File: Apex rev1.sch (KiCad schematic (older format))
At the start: 10 parts

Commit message: Update matrix and MCU
Updated matrix. Added decoupling capacitors. Added Encoder.
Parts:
- added C?: 1uF, symbol Device:C
- added C?: 4.7u, symbol Device:C_Small
- added C? (x4): .1u, symbol Device:C_Small
- added SW?: Rotary_Encoder, symbol Device:Rotary_Encoder
- R?: symbol keyboard_parts:R -> Apex-rev1-rescue:R-keyboard_parts
- SW?: symbol keyboard_parts:SW_PUSH -> Apex-rev1-rescue:SW_PUSH-keyboard_parts
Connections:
- net labels added: ENC1, ENC2
- wire segments 33 -> 49
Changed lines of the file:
@@
 	8400 1750 8250 1750
 $Comp
-L keyboard_parts:R R?
+L Apex-rev1-rescue:R-keyboard_parts R?
 U 1 1 5EFE3710
 P 8250 1500
@@
 Connection ~ 8250 1750
 $Comp
-L keyboard_parts:SW_PUSH SW?
+L Apex-rev1-rescue:SW_PUSH-keyboard_parts SW?
 U 1 1 5EFE4C93
 P 7800 1750
@@
 	8900 5450 8950 5450
 Wire Wire Line
-	8950 5450 8950 5500
+	8950 5450 8950 5800
 Connection ~ 8950 5450
 Wire Wire Line
@@
 L power:GND #PWR?
 U 1 1 5F0428AB
-P 8950 5500
-F 0 "#PWR?" H 8950 5250 50  0001 C CNN
-F 1 "GND" H 8955 5327 50  0000 C CNN
-F 2 "" H 8950 5500 50  0001 C CNN
-F 3 "" H 8950 5500 50  0001 C CNN
-	1    8950 5500
+P 8950 5800
+F 0 "#PWR?" H 8950 5550 50  0001 C CNN
+F 1 "GND" H 8955 5627 50  0000 C CNN
+F 2 "" H 8950 5800 50  0001 C CNN
+F 3 "" H 8950 5800 50  0001 C CNN
+	1    8950 5800
 	1    0    0    -1
 $EndComp
@@
 F1 "Key Matrix.sch" 50
 $EndSheet
+Wire Wire Line
+	8400 3050 7650 3050
+$Comp
+L Device:C C?
+U 1 1 5F07097E
+P 7650 3200
+F 0 "C?" H 7765 3246 50  0000 L CNN
+F 1 "1uF" H 7765 3155 50  0000 L CNN
+F 2 "" H 7688 3050 50  0001 C CNN
+F 3 "~" H 7650 3200 50  0001 C CNN
+	1    7650 3200
+	1    0    0    -1
+$EndComp
+Wire Wire Line
+	7650 3350 7650 3450
+$Comp
+L power:GND #PWR?
+U 1 1 5F071BD0
+P 7650 3450
+F 0 "#PWR?" H 7650 3200 50  0001 C CNN
+F 1 "GND" H 7655 3277 50  0000 C CNN
+F 2 "" H 7650 3450 50  0001 C CNN
+F 3 "" H 7650 3450 50  0001 C CNN
+	1    7650 3450
+	1    0    0    -1
+$EndComp
+Wire Wire Line
+	8400 2550 7950 2550
+Connection ~ 7950 2550
+Wire Wire Line
+	7950 2550 7150 2550
+$Comp
+L power:VCC #PWR?
+U 1 1 5F073B72
+P 7150 2550
+F 0 "#PWR?" H 7150 2400 50  0001 C CNN
+F 1 "VCC" H 7165 2723 50  0000 C CNN
+F 2 "" H 7150 2550 50  0001 C CNN
+F 3 "" H 7150 2550 50  0001 C CNN
+	1    7150 2550
+	1    0    0    -1
+$EndComp
+$Comp
+L Device:Rotary_Encoder SW?
+U 1 1 5F0786F9
+P 11700 2950
+F 0 "SW?" H 11930 2996 50  0000 L CNN
+F 1 "Rotary_Encoder" H 11930 2905 50  0000 L CNN
+F 2 "" H 11550 3110 50  0001 C CNN
+F 3 "~" H 11700 3210 50  0001 C CNN
+	1    11700 2950
+	1    0    0    -1
+$EndComp
+Text GLabel 11400 2850 0    50   Input ~ 0
+ENC1
+Text GLabel 11400 3050 0    50   Input ~ 0
+ENC2
+Wire Wire Line
+	11400 2950 11000 2950
+Wire Wire Line
+	11000 2950 11000 3100
+$Comp
+L power:GND #PWR?
+U 1 1 5F095086
+P 11000 3100
+F 0 "#PWR?" H 11000 2850 50  0001 C CNN
+F 1 "GND" H 11005 2927 50  0000 C CNN
+F 2 "" H 11000 3100 50  0001 C CNN
+F 3 "" H 11000 3100 50  0001 C CNN
+	1    11000 3100
+	1    0    0    -1
+$EndComp
+$Comp
+L Device:C_Small C?
+U 1 1 5F0A1E50
+P 5900 3250
+F 0 "C?" H 5992 3296 50  0000 L CNN
+F 1 "4.7u" H 5992 3205 50  0000 L CNN
+F 2 "" H 5900 3250 50  0001 C CNN
+F 3 "~" H 5900 3250 50  0001 C CNN
+	1    5900 3250
+	1    0    0    -1
+$EndComp
+$Comp
+L Device:C_Small C?
+U 1 1 5F0A2EEA
+P 5450 3250
+F 0 "C?" H 5542 3296 50  0000 L CNN
+F 1 ".1u" H 5542 3205 50  0000 L CNN
+F 2 "" H 5450 3250 50  0001 C CNN
+F 3 "~" H 5450 3250 50  0001 C CNN
+	1    5450 3250
+	1    0    0    -1
+$EndComp
+$Comp
+L Device:C_Small C?
+U 1 1 5F0A3767
+P 5000 3250
+F 0 "C?" H 5092 3296 50  0000 L CNN
+F 1 ".1u" H 5092 3205 50  0000 L CNN
+F 2 "" H 5000 3250 50  0001 C CNN
+F 3 "~" H 5000 3250 50  0001 C CNN
+	1    5000 3250
+	1    0    0    -1
+$EndComp
+$Comp
+L Device:C_Small C?
+U 1 1 5F0A3AEE
+P 4550 3250
+F 0 "C?" H 4642 3296 50  0000 L CNN
+F 1 ".1u" H 4642 3205 50  0000 L CNN
+F 2 "" H 4550 3250 50  0001 C CNN
+F 3 "~" H 4550 3250 50  0001 C CNN
+	1    4550 3250
+	1    0    0    -1
+$EndComp
+$Comp
+L Device:C_Small C?
+U 1 1 5F0A4338
+P 4200 3250
+F 0 "C?" H 4292 3296 50  0000 L CNN
+F 1 ".1u" H 4292 3205 50  0000 L CNN
+F 2 "" H 4200 3250 50  0001 C CNN
+F 3 "~" H 4200 3250 50  0001 C CNN
+	1    4200 3250
+	1    0    0    -1
+$EndComp
+Wire Wire Line
+	4200 3150 4550 3150
+Connection ~ 4550 3150
+Wire Wire Line
+	4550 3150 5000 3150
+Connection ~ 5000 3150
+Wire Wire Line
+	5000 3150 5450 3150
+Connection ~ 5450 3150
+Wire Wire Line
+	5450 3150 5900 3150
+Wire Wire Line
+	5900 3350 5450 3350
+Connection ~ 4550 3350
+Wire Wire Line
+	4550 3350 4200 3350
+Connection ~ 5000 3350
+Wire Wire Line
+	5000 3350 4550 3350
+Connection ~ 5450 3350
+Wire Wire Line
+	5450 3350 5000 3350
+Wire Wire Line
+	4200 3350 4200 3450
+Connection ~ 4200 3350
+Wire Wire Line
+	4200 3150 4200 3000
+Connection ~ 4200 3150
+$Comp
+L power:GND #PWR?
+U 1 1 5F0A7BB5
+P 4200 3450
+F 0 "#PWR?" H 4200 3200 50  0001 C CNN
+F 1 "GND" H 4205 3277 50  0000 C CNN
+F 2 "" H 4200 3450 50  0001 C CNN
+F 3 "" H 4200 3450 50  0001 C CNN
+	1    4200 3450
+	1    0    0    -1
+$EndComp
+$Comp
+L power:VCC #PWR?
+U 1 1 5F0A8382
+P 4200 3000
+F 0 "#PWR?" H 4200 2850 50  0001 C CNN
+F 1 "VCC" H 4215 3173 50  0000 C CNN
+F 2 "" H 4200 3000 50  0001 C CNN
+F 3 "" H 4200 3000 50  0001 C CNN
+	1    4200 3000
+	1    0    0    -1
+$EndComp
 $EndSCHEMATC

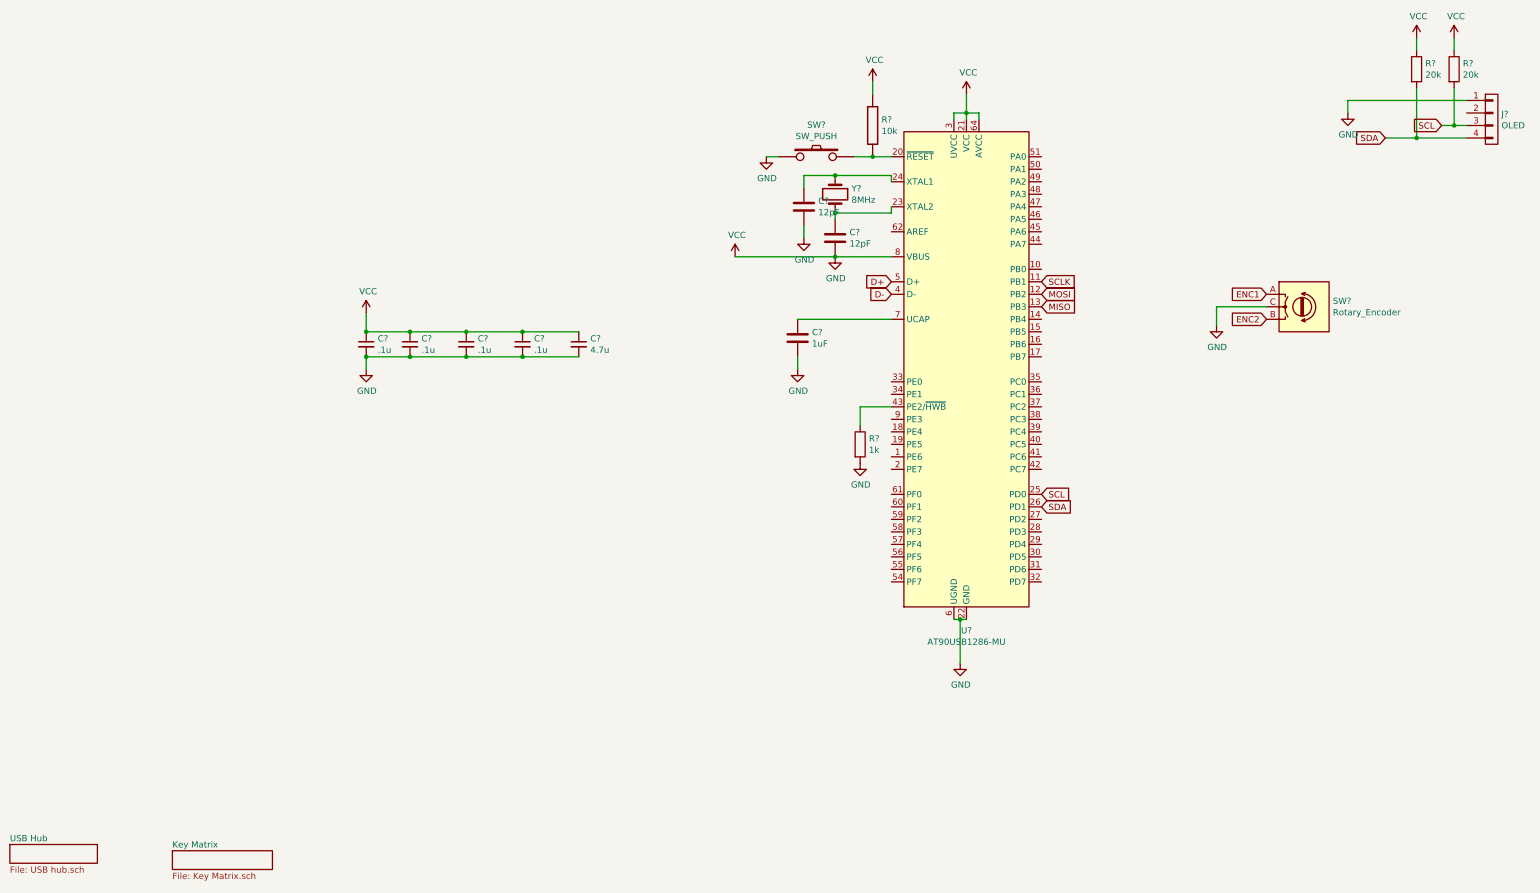
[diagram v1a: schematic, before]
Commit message: Begin annotation
Annotated schematic and began associating symbols with footprints.
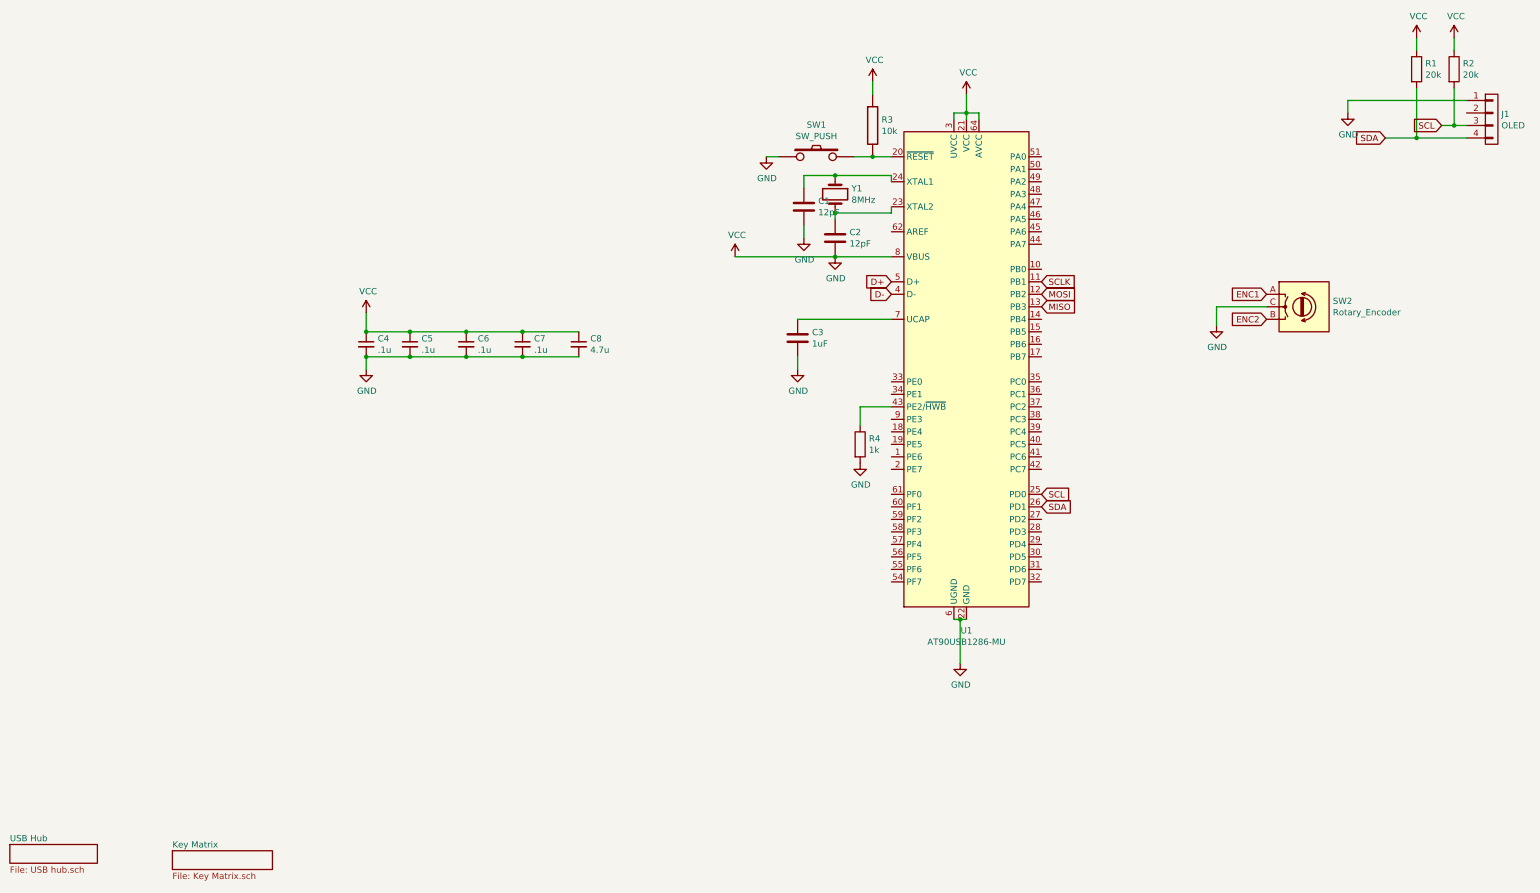
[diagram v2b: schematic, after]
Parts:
- C1, C2, C3, C4, C5, C6, C7, C8: renamed from C?; footprint (none) -> Capacitor_SMD:C_0805_2012Metric
- gave numbers to parts that had none: 9
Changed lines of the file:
@@
 $EndDescr
 $Comp
-L MCU_Microchip_AVR:AT90USB1286-MU U?
+L MCU_Microchip_AVR:AT90USB1286-MU U1
 U 1 1 5F010370
 P 9000 3450
-F 0 "U?" H 9000 1361 50  0000 C CNN
+F 0 "U1" H 9000 1361 50  0000 C CNN
 F 1 "AT90USB1286-MU" H 9000 1270 50  0000 C CNN
 F 2 "Package_DFN_QFN:QFN-64-1EP_9x9mm_P0.5mm_EP7.5x7.5mm" H 9000 3450 50  0001 C CIN
@@
 $EndComp
 $Comp
-L power:VCC #PWR?
+L power:VCC #PWR0101
 U 1 1 5F016D8A
 P 9000 1250
-F 0 "#PWR?" H 9000 1100 50  0001 C CNN
+F 0 "#PWR0101" H 9000 1100 50  0001 C CNN
 F 1 "VCC" H 9015 1423 50  0000 C CNN
 F 2 "" H 9000 1250 50  0001 C CNN
@@
 	8400 1750 8250 1750
 $Comp
-L Apex-rev1-rescue:R-keyboard_parts R?
+L Apex-rev1-rescue:R-keyboard_parts R3
 U 1 1 5EFE3710
 P 8250 1500
-F 0 "R?" H 8321 1546 50  0000 L CNN
+F 0 "R3" H 8321 1546 50  0000 L CNN
 F 1 "10k" H 8321 1455 50  0000 L CNN
-F 2 "" H 8250 1500 60  0000 C CNN
+F 2 "" H 8250 1500 60  0001 C CNN
 F 3 "" H 8250 1500 60  0000 C CNN
 	1    8250 1500
@@
 Connection ~ 8250 1750
 $Comp
-L Apex-rev1-rescue:SW_PUSH-keyboard_parts SW?
+L Apex-rev1-rescue:SW_PUSH-keyboard_parts SW1
 U 1 1 5EFE4C93
 P 7800 1750
-F 0 "SW?" H 7800 2005 50  0000 C CNN
+F 0 "SW1" H 7800 2005 50  0000 C CNN
 F 1 "SW_PUSH" H 7800 1914 50  0000 C CNN
-F 2 "" H 7800 1750 60  0000 C CNN
+F 2 "" H 7800 1750 60  0001 C CNN
 F 3 "" H 7800 1750 60  0000 C CNN
 	1    7800 1750
@@
 $EndComp
 $Comp
-L power:GND #PWR?
+L power:GND #PWR0102
 U 1 1 5EFE56D1
 P 7400 1750
-F 0 "#PWR?" H 7400 1500 50  0001 C CNN
+F 0 "#PWR0102" H 7400 1500 50  0001 C CNN
 F 1 "GND" H 7405 1577 50  0000 C CNN
 F 2 "" H 7400 1750 50  0001 C CNN
@@
 	8250 1250 8250 1150
 $Comp
-L power:VCC #PWR?
+L power:VCC #PWR0103
 U 1 1 5EFE6069
 P 8250 1150
-F 0 "#PWR?" H 8250 1000 50  0001 C CNN
+F 0 "#PWR0103" H 8250 1000 50  0001 C CNN
 F 1 "VCC" H 8265 1323 50  0000 C CNN
 F 2 "" H 8250 1150 50  0001 C CNN
@@
 	7400 1750 7500 1750
 $Comp
-L Device:Crystal Y?
+L Device:Crystal Y1
 U 1 1 5F03BFD9
 P 7950 2050
-F 0 "Y?" V 7904 2181 50  0000 L CNN
+F 0 "Y1" V 7904 2181 50  0000 L CNN
 F 1 "8MHz" V 7995 2181 50  0000 L CNN
 F 2 "" H 7950 2050 50  0001 C CNN
@@
 Connection ~ 7950 2200
 $Comp
-L Device:C C?
+L Device:C C1
 U 1 1 5F03FC8D
 P 7700 2150
-F 0 "C?" H 7815 2196 50  0000 L CNN
+F 0 "C1" H 7815 2196 50  0000 L CNN
 F 1 "12pF" H 7815 2105 50  0000 L CNN
-F 2 "" H 7738 2000 50  0001 C CNN
+F 2 "Capacitor_SMD:C_0805_2012Metric" H 7738 2000 50  0001 C CNN
 F 3 "~" H 7700 2150 50  0001 C CNN
 	1    7700 2150
@@
 	7700 2300 7700 2400
 $Comp
-L Device:C C?
+L Device:C C2
 U 1 1 5F0408BF
 P 7950 2400
-F 0 "C?" H 8065 2446 50  0000 L CNN
+F 0 "C2" H 8065 2446 50  0000 L CNN
 F 1 "12pF" H 8065 2355 50  0000 L CNN
-F 2 "" H 7988 2250 50  0001 C CNN
+F 2 "Capacitor_SMD:C_0805_2012Metric" H 7988 2250 50  0001 C CNN
 F 3 "~" H 7950 2400 50  0001 C CNN
 	1    7950 2400
@@
 $EndComp
 $Comp
-L power:GND #PWR?
+L power:GND #PWR0104
 U 1 1 5F0414EA
 P 7700 2400
-F 0 "#PWR?" H 7700 2150 50  0001 C CNN
+F 0 "#PWR0104" H 7700 2150 50  0001 C CNN
 F 1 "GND" H 7705 2227 50  0000 C CNN
 F 2 "" H 7700 2400 50  0001 C CNN
@@
 $EndComp
 $Comp
-L power:GND #PWR?
+L power:GND #PWR0105
 U 1 1 5F041BDD
 P 7950 2550
-F 0 "#PWR?" H 7950 2300 50  0001 C CNN
+F 0 "#PWR0105" H 7950 2300 50  0001 C CNN
 F 1 "GND" H 7955 2377 50  0000 C CNN
 F 2 "" H 7950 2550 50  0001 C CNN
@@
 	8950 5450 9000 5450
 $Comp
-L power:GND #PWR?
+L power:GND #PWR0106
 U 1 1 5F0428AB
 P 8950 5800
-F 0 "#PWR?" H 8950 5550 50  0001 C CNN
+F 0 "#PWR0106" H 8950 5550 50  0001 C CNN
 F 1 "GND" H 8955 5627 50  0000 C CNN
 F 2 "" H 8950 5800 50  0001 C CNN
@@
 	8150 3750 8150 3900
 $Comp
-L Device:R R?
+L Device:R R4
 U 1 1 5F0438EB
 P 8150 4050
-F 0 "R?" H 8220 4096 50  0000 L CNN
+F 0 "R4" H 8220 4096 50  0000 L CNN
 F 1 "1k" H 8220 4005 50  0000 L CNN
 F 2 "" V 8080 4050 50  0001 C CNN
@@
 $EndComp
 $Comp
-L power:GND #PWR?
+L power:GND #PWR0107
 U 1 1 5F0441E1
 P 8150 4200
-F 0 "#PWR?" H 8150 3950 50  0001 C CNN
+F 0 "#PWR0107" H 8150 3950 50  0001 C CNN
 F 1 "GND" H 8155 4027 50  0000 C CNN
 F 2 "" H 8150 4200 50  0001 C CNN
@@
 SDA
 $Comp
-L oled:OLED J?
+L oled:OLED J1
 U 1 1 5F05F2F8
 P 13200 1450
-F 0 "J?" H 13278 1491 50  0000 L CNN
+F 0 "J1" H 13278 1491 50  0000 L CNN
 F 1 "OLED" H 13278 1400 50  0000 L CNN
-F 2 "" H 13200 1450 50  0000 C CNN
+F 2 "" H 13200 1450 50  0001 C CNN
 F 3 "" H 13200 1450 50  0000 C CNN
 	1    13200 1450
@@
 	12050 1300 12050 1400
 $Comp
-L power:GND #PWR?
+L power:GND #PWR0108
 U 1 1 5F06312E
 P 12050 1400
-F 0 "#PWR?" H 12050 1150 50  0001 C CNN
+F 0 "#PWR0108" H 12050 1150 50  0001 C CNN
 F 1 "GND" H 12055 1227 50  0000 C CNN
 F 2 "" H 12050 1400 50  0001 C CNN
@@
 	12600 1600 12600 1200
 $Comp
-L Device:R R?
+L Device:R R1
 U 1 1 5F064810
 P 12600 1050
-F 0 "R?" H 12670 1096 50  0000 L CNN
+F 0 "R1" H 12670 1096 50  0000 L CNN
 F 1 "20k" H 12670 1005 50  0000 L CNN
 F 2 "" V 12530 1050 50  0001 C CNN
@@
 $EndComp
 $Comp
-L Device:R R?
+L Device:R R2
 U 1 1 5F067AAB
 P 12900 1050
-F 0 "R?" H 12970 1096 50  0000 L CNN
+F 0 "R2" H 12970 1096 50  0000 L CNN
 F 1 "20k" H 12970 1005 50  0000 L CNN
 F 2 "" V 12830 1050 50  0001 C CNN
@@
 	12900 900  12900 800
 $Comp
-L power:VCC #PWR?
+L power:VCC #PWR0109
 U 1 1 5F06AA70
 P 12600 800
-F 0 "#PWR?" H 12600 650 50  0001 C CNN
+F 0 "#PWR0109" H 12600 650 50  0001 C CNN
 F 1 "VCC" H 12615 973 50  0000 C CNN
 F 2 "" H 12600 800 50  0001 C CNN
@@
 $EndComp
 $Comp
-L power:VCC #PWR?
+L power:VCC #PWR0110
 U 1 1 5F06B137
 P 12900 800
-F 0 "#PWR?" H 12900 650 50  0001 C CNN
+F 0 "#PWR0110" H 12900 650 50  0001 C CNN
 F 1 "VCC" H 12915 973 50  0000 C CNN
 F 2 "" H 12900 800 50  0001 C CNN
@@
 	8400 3050 7650 3050
 $Comp
-L Device:C C?
+L Device:C C3
 U 1 1 5F07097E
 P 7650 3200
-F 0 "C?" H 7765 3246 50  0000 L CNN
+F 0 "C3" H 7765 3246 50  0000 L CNN
 F 1 "1uF" H 7765 3155 50  0000 L CNN
-F 2 "" H 7688 3050 50  0001 C CNN
+F 2 "Capacitor_SMD:C_0805_2012Metric" H 7688 3050 50  0001 C CNN
 F 3 "~" H 7650 3200 50  0001 C CNN
 	1    7650 3200
@@
 	7650 3350 7650 3450
 $Comp
-L power:GND #PWR?
+L power:GND #PWR0111
 U 1 1 5F071BD0
 P 7650 3450
-F 0 "#PWR?" H 7650 3200 50  0001 C CNN
+F 0 "#PWR0111" H 7650 3200 50  0001 C CNN
 F 1 "GND" H 7655 3277 50  0000 C CNN
 F 2 "" H 7650 3450 50  0001 C CNN
@@
 	7950 2550 7150 2550
 $Comp
-L power:VCC #PWR?
+L power:VCC #PWR0112
 U 1 1 5F073B72
 P 7150 2550
-F 0 "#PWR?" H 7150 2400 50  0001 C CNN
+F 0 "#PWR0112" H 7150 2400 50  0001 C CNN
 F 1 "VCC" H 7165 2723 50  0000 C CNN
 F 2 "" H 7150 2550 50  0001 C CNN
@@
 $EndComp
 $Comp
-L Device:Rotary_Encoder SW?
+L Device:Rotary_Encoder SW2
 U 1 1 5F0786F9
 P 11700 2950
-F 0 "SW?" H 11930 2996 50  0000 L CNN
+F 0 "SW2" H 11930 2996 50  0000 L CNN
 F 1 "Rotary_Encoder" H 11930 2905 50  0000 L CNN
 F 2 "" H 11550 3110 50  0001 C CNN
@@
 	11000 2950 11000 3100
 $Comp
-L power:GND #PWR?
+L power:GND #PWR0113
 U 1 1 5F095086
 P 11000 3100
-F 0 "#PWR?" H 11000 2850 50  0001 C CNN
+F 0 "#PWR0113" H 11000 2850 50  0001 C CNN
 F 1 "GND" H 11005 2927 50  0000 C CNN
 F 2 "" H 11000 3100 50  0001 C CNN
@@
 $EndComp
 $Comp
-L Device:C_Small C?
+L Device:C_Small C8
 U 1 1 5F0A1E50
 P 5900 3250
-F 0 "C?" H 5992 3296 50  0000 L CNN
+F 0 "C8" H 5992 3296 50  0000 L CNN
 F 1 "4.7u" H 5992 3205 50  0000 L CNN
-F 2 "" H 5900 3250 50  0001 C CNN
+F 2 "Capacitor_SMD:C_0805_2012Metric" H 5900 3250 50  0001 C CNN
 F 3 "~" H 5900 3250 50  0001 C CNN
 	1    5900 3250
@@
 $EndComp
 $Comp
-L Device:C_Small C?
+L Device:C_Small C7
 U 1 1 5F0A2EEA
 P 5450 3250
-F 0 "C?" H 5542 3296 50  0000 L CNN
+F 0 "C7" H 5542 3296 50  0000 L CNN
 F 1 ".1u" H 5542 3205 50  0000 L CNN
-F 2 "" H 5450 3250 50  0001 C CNN
+F 2 "Capacitor_SMD:C_0805_2012Metric" H 5450 3250 50  0001 C CNN
 F 3 "~" H 5450 3250 50  0001 C CNN
 	1    5450 3250
@@
 $EndComp
 $Comp
-L Device:C_Small C?
+L Device:C_Small C6
 U 1 1 5F0A3767
 P 5000 3250
-F 0 "C?" H 5092 3296 50  0000 L CNN
+F 0 "C6" H 5092 3296 50  0000 L CNN
 F 1 ".1u" H 5092 3205 50  0000 L CNN
-F 2 "" H 5000 3250 50  0001 C CNN
+F 2 "Capacitor_SMD:C_0805_2012Metric" H 5000 3250 50  0001 C CNN
 F 3 "~" H 5000 3250 50  0001 C CNN
 	1    5000 3250
@@
 $EndComp
 $Comp
-L Device:C_Small C?
+L Device:C_Small C5
 U 1 1 5F0A3AEE
 P 4550 3250
-F 0 "C?" H 4642 3296 50  0000 L CNN
+F 0 "C5" H 4642 3296 50  0000 L CNN
 F 1 ".1u" H 4642 3205 50  0000 L CNN
-F 2 "" H 4550 3250 50  0001 C CNN
+F 2 "Capacitor_SMD:C_0805_2012Metric" H 4550 3250 50  0001 C CNN
 F 3 "~" H 4550 3250 50  0001 C CNN
 	1    4550 3250
@@
 $EndComp
 $Comp
-L Device:C_Small C?
+L Device:C_Small C4
 U 1 1 5F0A4338
 P 4200 3250
-F 0 "C?" H 4292 3296 50  0000 L CNN
+F 0 "C4" H 4292 3296 50  0000 L CNN
 F 1 ".1u" H 4292 3205 50  0000 L CNN
-F 2 "" H 4200 3250 50  0001 C CNN
+F 2 "Capacitor_SMD:C_0805_2012Metric" H 4200 3250 50  0001 C CNN
 F 3 "~" H 4200 3250 50  0001 C CNN
 	1    4200 3250
@@
 Connection ~ 4200 3150
 $Comp
-L power:GND #PWR?
+L power:GND #PWR0114
 U 1 1 5F0A7BB5
 P 4200 3450
-F 0 "#PWR?" H 4200 3200 50  0001 C CNN
+F 0 "#PWR0114" H 4200 3200 50  0001 C CNN
 F 1 "GND" H 4205 3277 50  0000 C CNN
 F 2 "" H 4200 3450 50  0001 C CNN
@@
 $EndComp
 $Comp
-L power:VCC #PWR?
+L power:VCC #PWR0115
 U 1 1 5F0A8382
 P 4200 3000
-F 0 "#PWR?" H 4200 2850 50  0001 C CNN
+F 0 "#PWR0115" H 4200 2850 50  0001 C CNN
 F 1 "VCC" H 4215 3173 50  0000 C CNN
 F 2 "" H 4200 3000 50  0001 C CNN
